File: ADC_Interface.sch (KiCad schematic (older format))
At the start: 19 parts, among them U3 ADS131M04, Y3 8.192 MHz

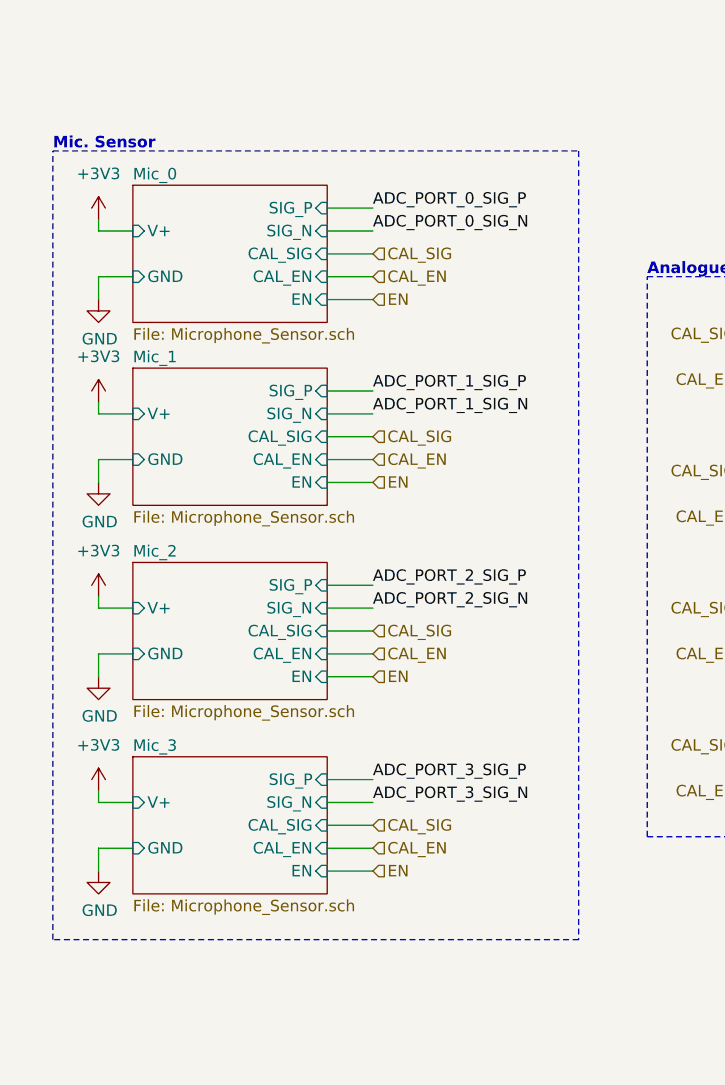
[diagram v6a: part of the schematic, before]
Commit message: CHange to single 3 designs to save cost
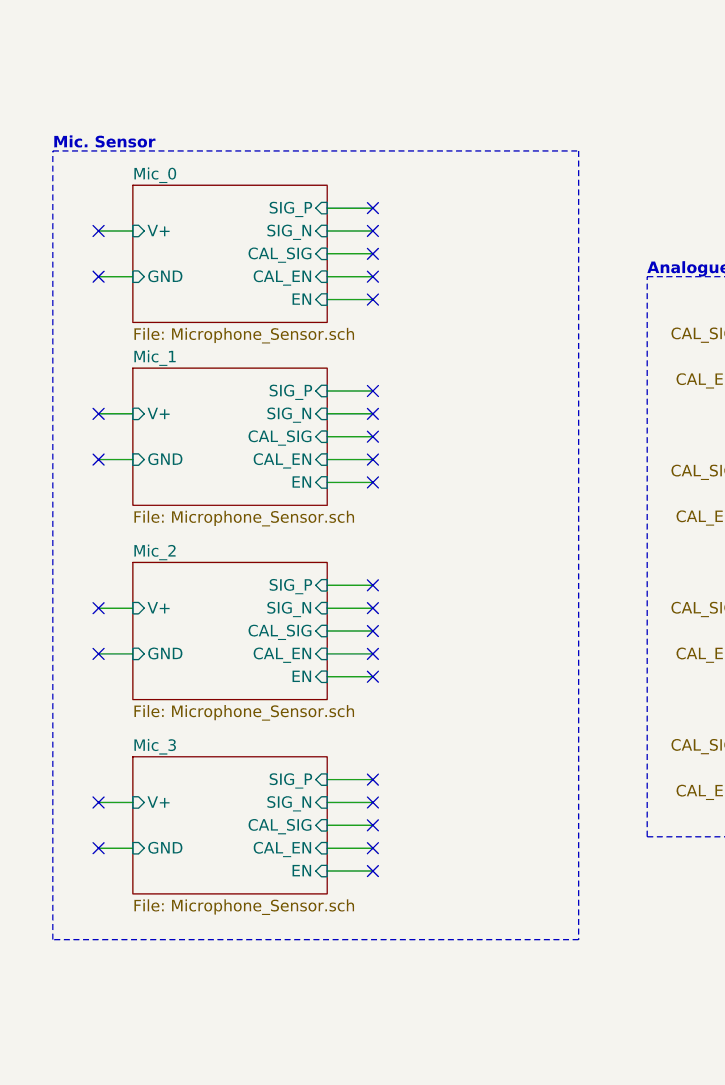
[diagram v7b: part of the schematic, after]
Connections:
- no-connect marks 0 -> 28
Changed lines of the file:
@@
 Text Label 4900 6000 0    50   ~ 0
 ADC_PORT_3_SIG_N
-$Comp
-L power:+3V3 #PWR040
-U 1 1 5EF1ACF8
-P 1050 3600
-F 0 "#PWR040" H 1050 3450 50  0001 C CNN
-F 1 "+3V3" H 1050 3800 50  0000 C CNN
-F 2 "" H 1050 3600 50  0001 C CNN
-F 3 "" H 1050 3600 50  0001 C CNN
-	1    1050 3600
-	1    0    0    -1
-$EndComp
-$Comp
-L power:GND #PWR041
-U 1 1 5EF1B2BC
-P 1050 3950
-F 0 "#PWR041" H 1050 3700 50  0001 C CNN
-F 1 "GND" H 1055 3777 50  0000 C CNN
-F 2 "" H 1050 3950 50  0001 C CNN
-F 3 "" H 1050 3950 50  0001 C CNN
-	1    1050 3950
-	1    0    0    -1
-$EndComp
-Text Label 2250 3650 0    50   ~ 0
-ADC_PORT_0_SIG_N
-Text Label 2250 3550 0    50   ~ 0
-ADC_PORT_0_SIG_P
-Text Label 2250 4350 0    50   ~ 0
-ADC_PORT_1_SIG_P
-Text Label 2250 4450 0    50   ~ 0
-ADC_PORT_1_SIG_N
 Wire Wire Line
 	2250 4350 2050 4350
@@
 Text HLabel 3900 6100 0    50   Input ~ 0
 CAL_EN
-Text HLabel 2250 3750 2    50   Input ~ 0
-CAL_SIG
 Wire Wire Line
 	2250 3850 2050 3850
-Text HLabel 2250 3850 2    50   Input ~ 0
-CAL_EN
 Wire Wire Line
 	2250 3950 2050 3950
@@
 F8 "CAL_SIG" I R 2050 4550 50
 $EndSheet
-Text HLabel 2250 4550 2    50   Input ~ 0
-CAL_SIG
-Text HLabel 2250 4650 2    50   Input ~ 0
-CAL_EN
 Wire Wire Line
 	2250 4650 2050 4650
@@
 	2250 4750 2050 4750
 Wire Wire Line
-	1200 3650 1050 3650
-Wire Wire Line
-	1050 3650 1050 3600
-Wire Wire Line
-	1200 3850 1050 3850
-Wire Wire Line
-	1050 3850 1050 3950
-$Comp
-L power:+3V3 #PWR042
-U 1 1 5EF863E3
-P 1050 4400
-F 0 "#PWR042" H 1050 4250 50  0001 C CNN
-F 1 "+3V3" H 1050 4600 50  0000 C CNN
-F 2 "" H 1050 4400 50  0001 C CNN
-F 3 "" H 1050 4400 50  0001 C CNN
-	1    1050 4400
-	1    0    0    -1
-$EndComp
-$Comp
-L power:GND #PWR043
-U 1 1 5EF863E9
-P 1050 4750
-F 0 "#PWR043" H 1050 4500 50  0001 C CNN
-F 1 "GND" H 1055 4577 50  0000 C CNN
-F 2 "" H 1050 4750 50  0001 C CNN
-F 3 "" H 1050 4750 50  0001 C CNN
-	1    1050 4750
-	1    0    0    -1
-$EndComp
-Wire Wire Line
 	1200 4450 1050 4450
 Wire Wire Line
-	1050 4450 1050 4400
-Wire Wire Line
 	1200 4650 1050 4650
-Wire Wire Line
-	1050 4650 1050 4750
 Wire Wire Line
 	3900 6100 4000 6100
@@
 Text HLabel 4900 6100 2    50   Input ~ 0
 EN
-Text HLabel 2250 4750 2    50   Input ~ 0
-EN
-Text HLabel 2250 3950 2    50   Input ~ 0
-EN
-Text HLabel 2250 5600 2    50   Input ~ 0
-EN
-Text HLabel 2250 6450 2    50   Input ~ 0
-EN
-Wire Wire Line
-	1050 6350 1050 6450
 Wire Wire Line
 	1200 6350 1050 6350
 Wire Wire Line
-	1050 6150 1050 6100
-Wire Wire Line
 	1200 6150 1050 6150
-$Comp
-L power:GND #PWR047
-U 1 1 5F0090D7
-P 1050 6450
-F 0 "#PWR047" H 1050 6200 50  0001 C CNN
-F 1 "GND" H 1055 6277 50  0000 C CNN
-F 2 "" H 1050 6450 50  0001 C CNN
-F 3 "" H 1050 6450 50  0001 C CNN
-	1    1050 6450
-	1    0    0    -1
-$EndComp
-$Comp
-L power:+3V3 #PWR046
-U 1 1 5F0090D1
-P 1050 6100
-F 0 "#PWR046" H 1050 5950 50  0001 C CNN
-F 1 "+3V3" H 1050 6300 50  0000 C CNN
-F 2 "" H 1050 6100 50  0001 C CNN
-F 3 "" H 1050 6100 50  0001 C CNN
-	1    1050 6100
-	1    0    0    -1
-$EndComp
-Wire Wire Line
-	2250 6450 2050 6450
-Wire Wire Line
-	2250 6350 2050 6350
-Text HLabel 2250 6350 2    50   Input ~ 0
-CAL_EN
-Text HLabel 2250 6250 2    50   Input ~ 0
-CAL_SIG
 $Sheet
 S 1200 5950 850  600
@@
 $EndSheet
 Wire Wire Line
-	2250 6250 2050 6250
-Wire Wire Line
-	2250 6150 2050 6150
-Wire Wire Line
-	2250 6050 2050 6050
-Text Label 2250 6150 0    50   ~ 0
-ADC_PORT_3_SIG_N
-Text Label 2250 6050 0    50   ~ 0
-ADC_PORT_3_SIG_P
-Wire Wire Line
-	1050 5500 1050 5600
-Wire Wire Line
 	1200 5500 1050 5500
 Wire Wire Line
-	1050 5300 1050 5250
-Wire Wire Line
 	1200 5300 1050 5300
-$Comp
-L power:GND #PWR045
-U 1 1 5F0013F5
-P 1050 5600
-F 0 "#PWR045" H 1050 5350 50  0001 C CNN
-F 1 "GND" H 1055 5427 50  0000 C CNN
-F 2 "" H 1050 5600 50  0001 C CNN
-F 3 "" H 1050 5600 50  0001 C CNN
-	1    1050 5600
-	1    0    0    -1
-$EndComp
-$Comp
-L power:+3V3 #PWR044
-U 1 1 5F0013EF
-P 1050 5250
-F 0 "#PWR044" H 1050 5100 50  0001 C CNN
-F 1 "+3V3" H 1050 5450 50  0000 C CNN
-F 2 "" H 1050 5250 50  0001 C CNN
-F 3 "" H 1050 5250 50  0001 C CNN
-	1    1050 5250
-	1    0    0    -1
-$EndComp
 Wire Wire Line
 	2250 5600 2050 5600
 Wire Wire Line
 	2250 5500 2050 5500
-Text HLabel 2250 5500 2    50   Input ~ 0
-CAL_EN
-Text HLabel 2250 5400 2    50   Input ~ 0
-CAL_SIG
 $Sheet
 S 1200 5100 850  600
@@
 Wire Wire Line
 	2250 5200 2050 5200
-Text Label 2250 5300 0    50   ~ 0
-ADC_PORT_2_SIG_N
-Text Label 2250 5200 0    50   ~ 0
-ADC_PORT_2_SIG_P
 Wire Wire Line
 	9350 3300 9500 3300
@@
 Wire Wire Line
 	9800 3200 10050 3200
+NoConn ~ 2250 4350
+NoConn ~ 2250 4450
+NoConn ~ 2250 4550
+NoConn ~ 2250 4650
+NoConn ~ 2250 4750
+Wire Wire Line
+	2250 6450 2050 6450
+Wire Wire Line
+	2250 6350 2050 6350
+Wire Wire Line
+	2250 6250 2050 6250
+Wire Wire Line
+	2250 6150 2050 6150
+Wire Wire Line
+	2250 6050 2050 6050
+NoConn ~ 2250 6050
+NoConn ~ 2250 6150
+NoConn ~ 2250 6250
+NoConn ~ 2250 6350
+NoConn ~ 2250 6450
+NoConn ~ 2250 3550
+NoConn ~ 2250 3650
+NoConn ~ 2250 3750
+NoConn ~ 2250 3850
+NoConn ~ 2250 3950
+NoConn ~ 2250 5200
+NoConn ~ 2250 5300
+NoConn ~ 2250 5400
+NoConn ~ 2250 5500
+NoConn ~ 2250 5600
+Wire Wire Line
+	1200 3850 1050 3850
+Wire Wire Line
+	1200 3650 1050 3650
+NoConn ~ 1050 6350
+NoConn ~ 1050 6150
+NoConn ~ 1050 5500
+NoConn ~ 1050 5300
+NoConn ~ 1050 4650
+NoConn ~ 1050 4450
+NoConn ~ 1050 3850
+NoConn ~ 1050 3650
 $EndSCHEMATC

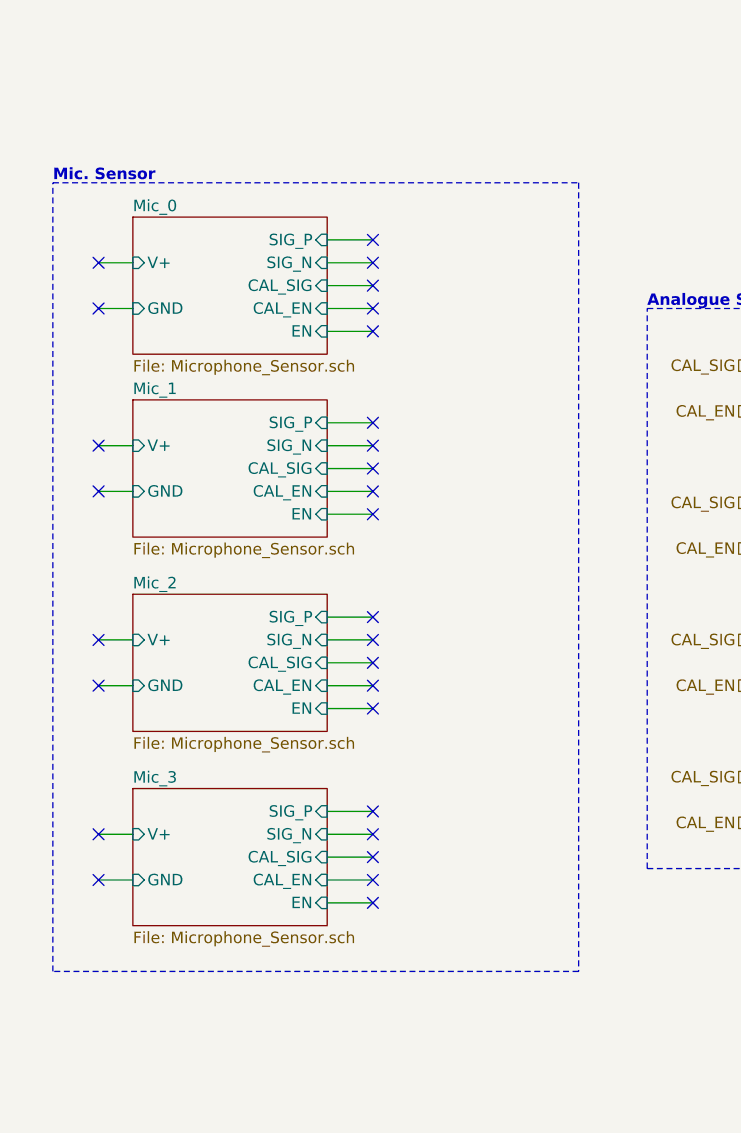
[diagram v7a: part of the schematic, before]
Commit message: Remove Mic. board
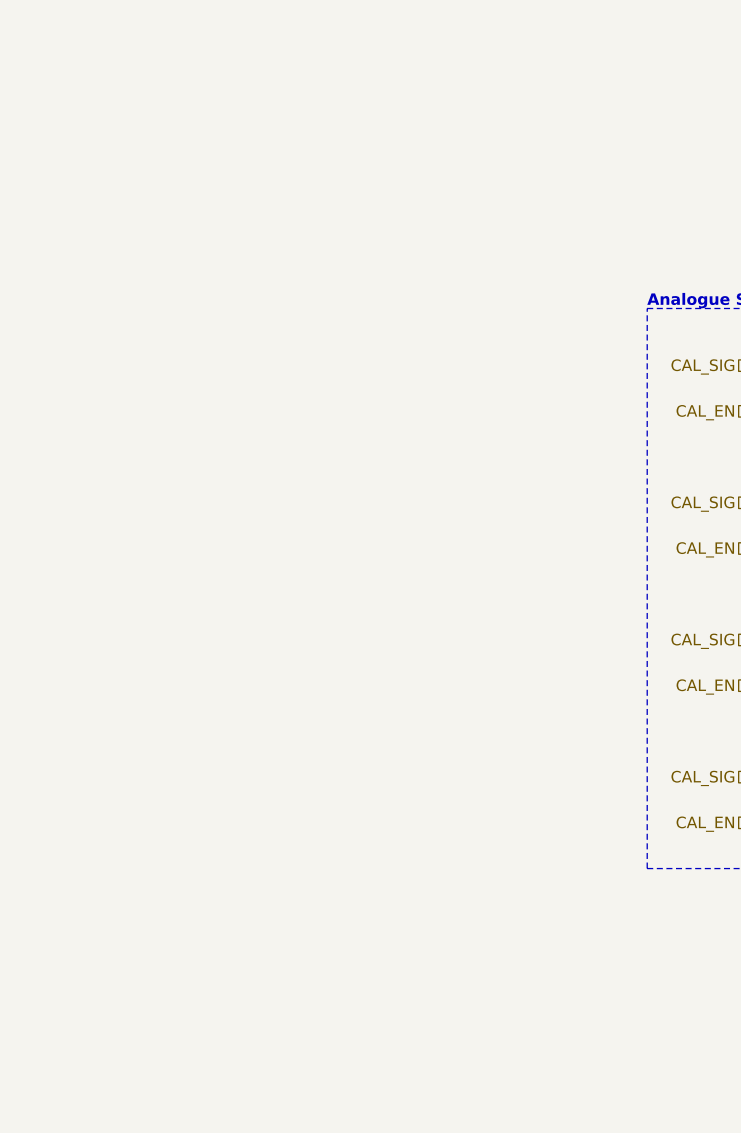
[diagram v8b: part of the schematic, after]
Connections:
- no-connect marks 28 -> 0
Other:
- note removed: "Mic. Sensor"
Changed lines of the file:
@@
 $Descr A4 11693 8268
 encoding utf-8
-Sheet 2 17
+Sheet 2 13
 Title "Kleinvoet"
 Date "2020-06-11"
@@
 Wire Wire Line
 	4650 4700 6150 4700
-$Sheet
-S 1200 3450 850  600
-U 5EECE6B8
-F0 "Mic_0" 50
-F1 "Microphone_Sensor.sch" 50
-F2 "V+" I L 1200 3650 50
-F3 "GND" I L 1200 3850 50
-F4 "SIG_P" I R 2050 3550 50
-F5 "SIG_N" I R 2050 3650 50
-F6 "EN" I R 2050 3950 50
-F7 "CAL_EN" I R 2050 3850 50
-F8 "CAL_SIG" I R 2050 3750 50
-$EndSheet
 Text Label 4900 4200 0    50   ~ 0
 ADC_PORT_0_SIG_N
@@
 Text Label 4900 6000 0    50   ~ 0
 ADC_PORT_3_SIG_N
-Wire Wire Line
-	2250 4350 2050 4350
-Wire Wire Line
-	2250 4450 2050 4450
-Wire Wire Line
-	2250 4550 2050 4550
-Wire Wire Line
-	2250 3750 2050 3750
-Wire Wire Line
-	2250 3650 2050 3650
-Wire Wire Line
-	2250 3550 2050 3550
-Text Notes 850  3300 0    50   ~ 10
-Mic. Sensor
 Wire Wire Line
 	800  1250 800  1350
@@
 CAL_EN
 Wire Wire Line
-	2250 3850 2050 3850
-Wire Wire Line
-	2250 3950 2050 3950
-$Sheet
-S 1200 4250 850  600
-U 5EF4C631
-F0 "Mic_1" 50
-F1 "Microphone_Sensor.sch" 50
-F2 "V+" I L 1200 4450 50
-F3 "GND" I L 1200 4650 50
-F4 "SIG_P" I R 2050 4350 50
-F5 "SIG_N" I R 2050 4450 50
-F6 "EN" I R 2050 4750 50
-F7 "CAL_EN" I R 2050 4650 50
-F8 "CAL_SIG" I R 2050 4550 50
-$EndSheet
-Wire Wire Line
-	2250 4650 2050 4650
-Wire Wire Line
-	2250 4750 2050 4750
-Wire Wire Line
-	1200 4450 1050 4450
-Wire Wire Line
-	1200 4650 1050 4650
-Wire Wire Line
 	3900 6100 4000 6100
 Wire Wire Line
@@
 Wire Notes Line
 	3450 6300 5650 6300
-Wire Notes Line
-	3150 6750 850  6750
-Wire Notes Line
-	850  6750 850  3300
-Wire Notes Line
-	850  3300 3150 3300
-Wire Notes Line
-	3150 3300 3150 6750
 Text HLabel 4900 4300 2    50   Input ~ 0
 EN
@@
 Text HLabel 4900 6100 2    50   Input ~ 0
 EN
-Wire Wire Line
-	1200 6350 1050 6350
-Wire Wire Line
-	1200 6150 1050 6150
-$Sheet
-S 1200 5950 850  600
-U 5F0090C7
-F0 "Mic_3" 50
-F1 "Microphone_Sensor.sch" 50
-F2 "V+" I L 1200 6150 50
-F3 "GND" I L 1200 6350 50
-F4 "SIG_P" I R 2050 6050 50
-F5 "SIG_N" I R 2050 6150 50
-F6 "EN" I R 2050 6450 50
-F7 "CAL_EN" I R 2050 6350 50
-F8 "CAL_SIG" I R 2050 6250 50
-$EndSheet
-Wire Wire Line
-	1200 5500 1050 5500
-Wire Wire Line
-	1200 5300 1050 5300
-Wire Wire Line
-	2250 5600 2050 5600
-Wire Wire Line
-	2250 5500 2050 5500
-$Sheet
-S 1200 5100 850  600
-U 5F0013E5
-F0 "Mic_2" 50
-F1 "Microphone_Sensor.sch" 50
-F2 "V+" I L 1200 5300 50
-F3 "GND" I L 1200 5500 50
-F4 "SIG_P" I R 2050 5200 50
-F5 "SIG_N" I R 2050 5300 50
-F6 "EN" I R 2050 5600 50
-F7 "CAL_EN" I R 2050 5500 50
-F8 "CAL_SIG" I R 2050 5400 50
-$EndSheet
-Wire Wire Line
-	2250 5400 2050 5400
-Wire Wire Line
-	2250 5300 2050 5300
-Wire Wire Line
-	2250 5200 2050 5200
 Wire Wire Line
 	9350 3300 9500 3300
@@
 Wire Wire Line
 	9800 3200 10050 3200
-NoConn ~ 2250 4350
-NoConn ~ 2250 4450
-NoConn ~ 2250 4550
-NoConn ~ 2250 4650
-NoConn ~ 2250 4750
-Wire Wire Line
-	2250 6450 2050 6450
-Wire Wire Line
-	2250 6350 2050 6350
-Wire Wire Line
-	2250 6250 2050 6250
-Wire Wire Line
-	2250 6150 2050 6150
-Wire Wire Line
-	2250 6050 2050 6050
-NoConn ~ 2250 6050
-NoConn ~ 2250 6150
-NoConn ~ 2250 6250
-NoConn ~ 2250 6350
-NoConn ~ 2250 6450
-NoConn ~ 2250 3550
-NoConn ~ 2250 3650
-NoConn ~ 2250 3750
-NoConn ~ 2250 3850
-NoConn ~ 2250 3950
-NoConn ~ 2250 5200
-NoConn ~ 2250 5300
-NoConn ~ 2250 5400
-NoConn ~ 2250 5500
-NoConn ~ 2250 5600
-Wire Wire Line
-	1200 3850 1050 3850
-Wire Wire Line
-	1200 3650 1050 3650
-NoConn ~ 1050 6350
-NoConn ~ 1050 6150
-NoConn ~ 1050 5500
-NoConn ~ 1050 5300
-NoConn ~ 1050 4650
-NoConn ~ 1050 4450
-NoConn ~ 1050 3850
-NoConn ~ 1050 3650
 $EndSCHEMATC
